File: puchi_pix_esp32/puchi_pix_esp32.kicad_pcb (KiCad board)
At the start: 2 copper layers, 40.3 x 40.3 mm, 41 parts, among them J1 USB_C_Receptacle_USB2.0_16P, J2 Conn_01x08, J3 JST-PH, J4 Conn_01x04_Socket, SW1 BOOT, SW2 RST, U1 ESP32-C3-MINI-1, U2 MCP73831-2-OT, U3 KXTJ3-1057, U4 AP2112K-3.3

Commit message: Update D1 to green LED (C12624) with R3=4.7k and add production files
Co-Authored-By: Claude Opus 4.6 (1M context) <noreply@anthropic.com>
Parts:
- R3: value 39 -> 4.7k
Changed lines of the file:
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@@
 			)
 		)
-		(property "Value" "39"
+		(property "Value" "4.7k"
 			(at 0 1.17 90)
 			(layer "F.Fab")
@@
 			)
 		)
-		(property "LCSC" "C25110"
+		(property "LCSC" "C25900"
 			(at 0 0 90)
 			(unlocked yes)
@@
 		(sheetname "/")
 		(sheetfile "puchi_pix_esp32.kicad_sch")
-		(attr through_hole exclude_from_bom)
+		(attr through_hole exclude_from_pos_files exclude_from_bom)
 		(fp_line
 			(start -1.33 1.27)
@@
 			)
 		)
-		(property "LCSC" "C72041"
+		(property "LCSC" "C12624"
 			(at 0 0 90)
 			(unlocked yes)

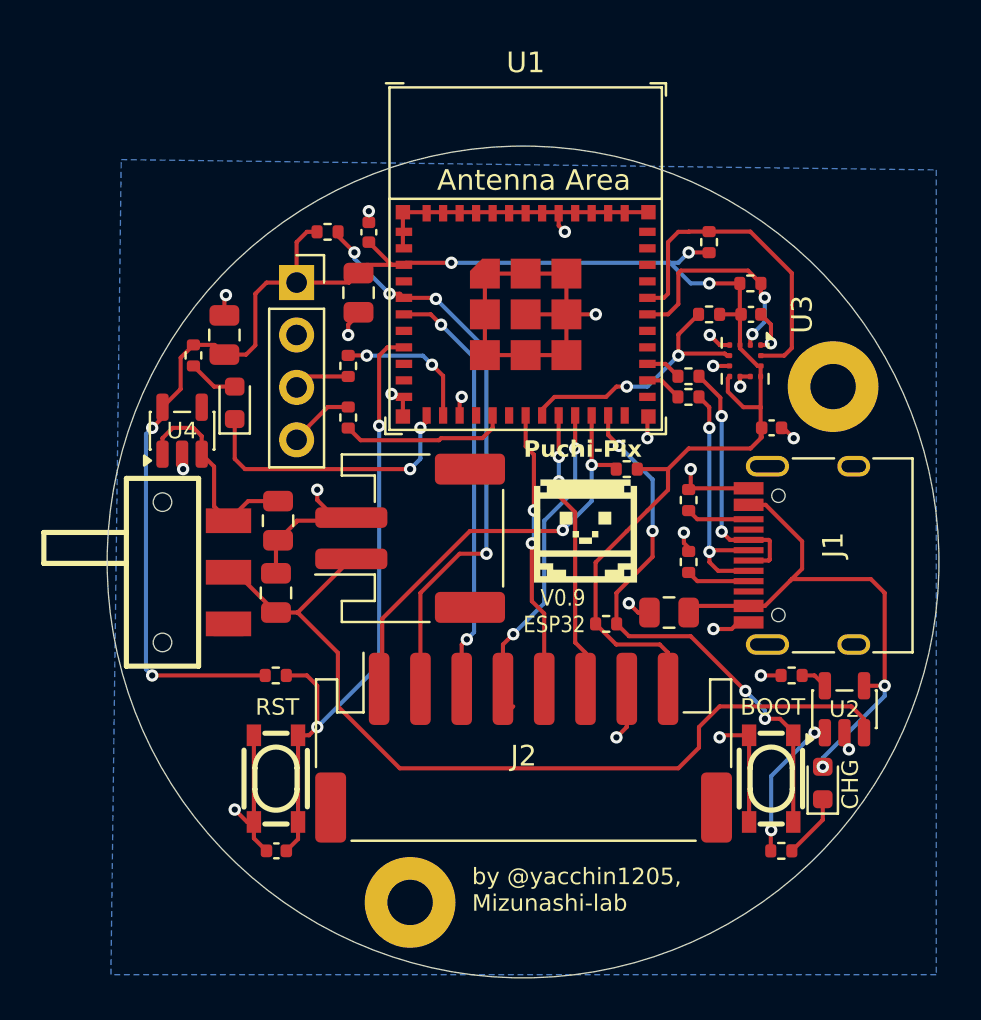
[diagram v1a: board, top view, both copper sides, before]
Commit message: Finalize puchi_pix/esp32 layout and regenerate JLCPCB production files (puchi_pix V0_95)
Co-Authored-By: Claude Opus 4.8 (1M context) <noreply@anthropic.com>
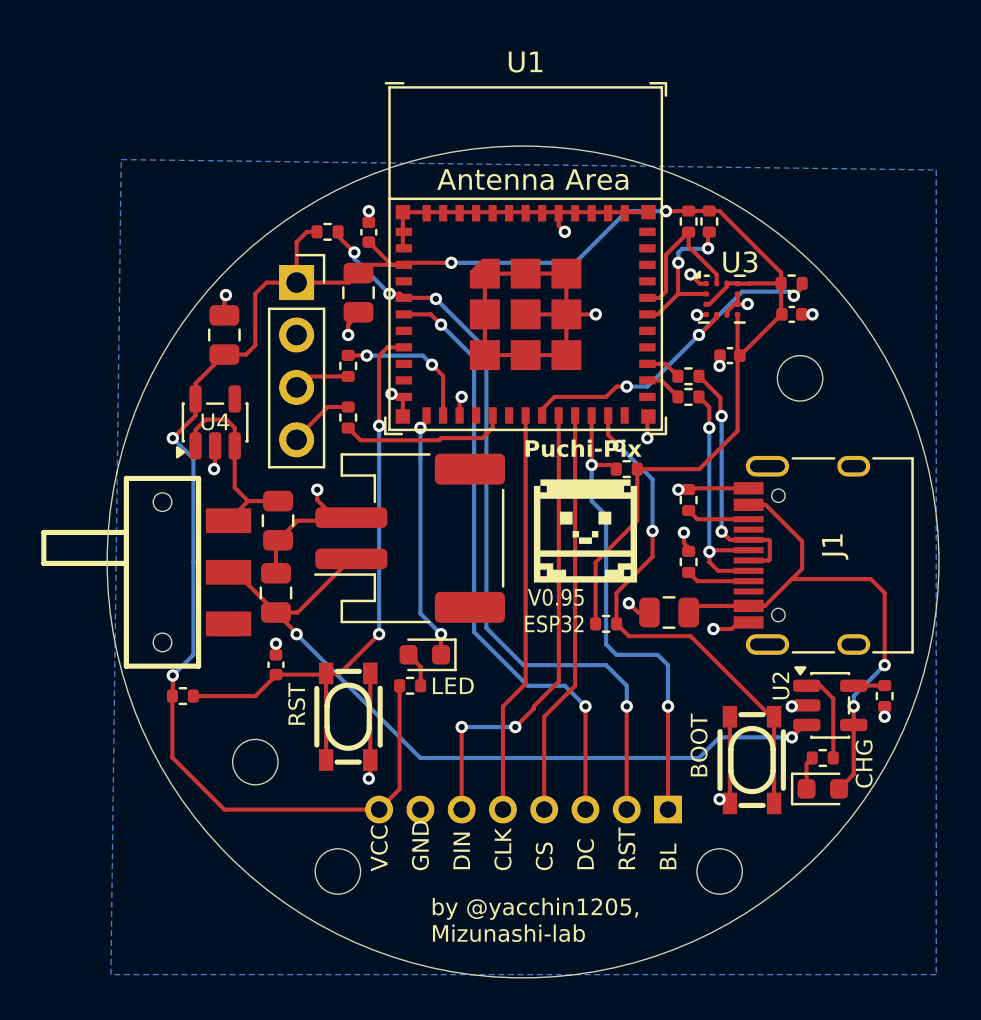
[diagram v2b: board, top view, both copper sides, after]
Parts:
- removed the REF** at (89.0, 94.5)
- removed the REF** at (109.5, 69.5)
- added REF**: MountingHole_2.2mm_M2, MountingHole:MountingHole_2.2mm_M2, F.Cu at (104.0, 93.0)
- added REF**: MountingHole_2.2mm_M2, MountingHole:MountingHole_2.2mm_M2, F.Cu at (107.9, 69.1)
- added REF**: MountingHole_2.2mm_M2, MountingHole:MountingHole_2.2mm_M2, F.Cu at (81.5, 87.7)
- added REF**: MountingHole_2.2mm_M2, MountingHole:MountingHole_2.2mm_M2, F.Cu at (85.5, 93.0)
- J2: value Conn_01x08 -> Conn_01x08_Socket; footprint Connector_JST:JST_PH_S8B-PH-SM4-TB_1x08-1MP_P2.00mm_Horizontal -> Connector_PinSocket_2.00mm:PinSocket_1x08_P2.00mm_Vertical; moved to B.Cu
- moved R3 19.1 mm to (89.0, 84.0), turned to 180 degrees
- moved D1 15.3 mm to (89.7, 82.5), turned to 180 degrees
- moved C1 9.02 mm to (82.5, 83.0), turned to 90 degrees
- moved J2 7.62 mm to (101.5, 90.0), turned to 90 degrees
- moved R11 4.93 mm to (109.0, 87.5), turned to 180 degrees
- moved R10 4.62 mm to (112.0, 84.5), turned to -90 degrees
- moved R2 4.61 mm to (78.0, 84.5)
- moved SW2 4.61 mm to (86.0, 85.5), turned to 90 degrees
- moved R16 4.27 mm to (107.5, 64.5), turned to 180 degrees
- moved C9 4.04 mm to (104.5, 68.0), turned to 180 degrees
- moved R13 3.60 mm to (103.5, 61.5), turned to -90 degrees
- moved U3 3.19 mm to (104.1, 65.3), turned to 0 degrees
- moved C8 1.98 mm to (107.5, 66.0)
- moved U4 1.65 mm to (79.5, 71.2)
- moved R12 1.41 mm to (102.5, 61.5), turned to -90 degrees
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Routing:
- net /DC: track 20.3 -> 29.7 mm
- net +3.3V: track 96.2 -> 105.4 mm, vias 5 -> 4
- net /RST: track 28.4 -> 37.5 mm
- net /DIN: track 13.8 -> 22.8 mm
- net Net-(U1-GPIO21/U0TXD): track 15.9 -> 7.42 mm
- net GND: track 80.9 -> 74.2 mm
- net Net-(J3-Pin_1): track 42.7 -> 37.2 mm, vias 0 -> 2
- net /CLK: track 13.7 -> 19.1 mm, vias 2 -> 0
- net /CS: track 15.2 -> 19.9 mm, vias 2 -> 0
- net Net-(U1-GPIO5/ADC2_CH0): track 12.9 -> 17.1 mm, vias 2 -> 3
- net Net-(U1-GPIO20/U0RXD): track 10.9 -> 7.57 mm
- net Net-(U2-STAT): track 6.60 -> 4.42 mm, vias 2 -> 0
- net Net-(U1-EN/CHIP_PU): track 31.2 -> 29.3 mm
- net Net-(D1-K): track 13.7 -> 12.2 mm
- net Net-(CHG1-K): track 3.12 -> 1.61 mm
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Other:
- board text added: "BL"
- board text added: "CLK"
- board text added: "CS"
- board text added: "DC"
- board text added: "DIN"
- board text added: "LED"
- board text added: "V0.95 ESP32"
- board text added: "VCC"
- board text removed: "V0.9 ESP32"
